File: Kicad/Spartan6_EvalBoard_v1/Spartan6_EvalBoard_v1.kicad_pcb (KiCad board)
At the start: 2 copper layers, 1 part, among them CON1 USB-MINI-B

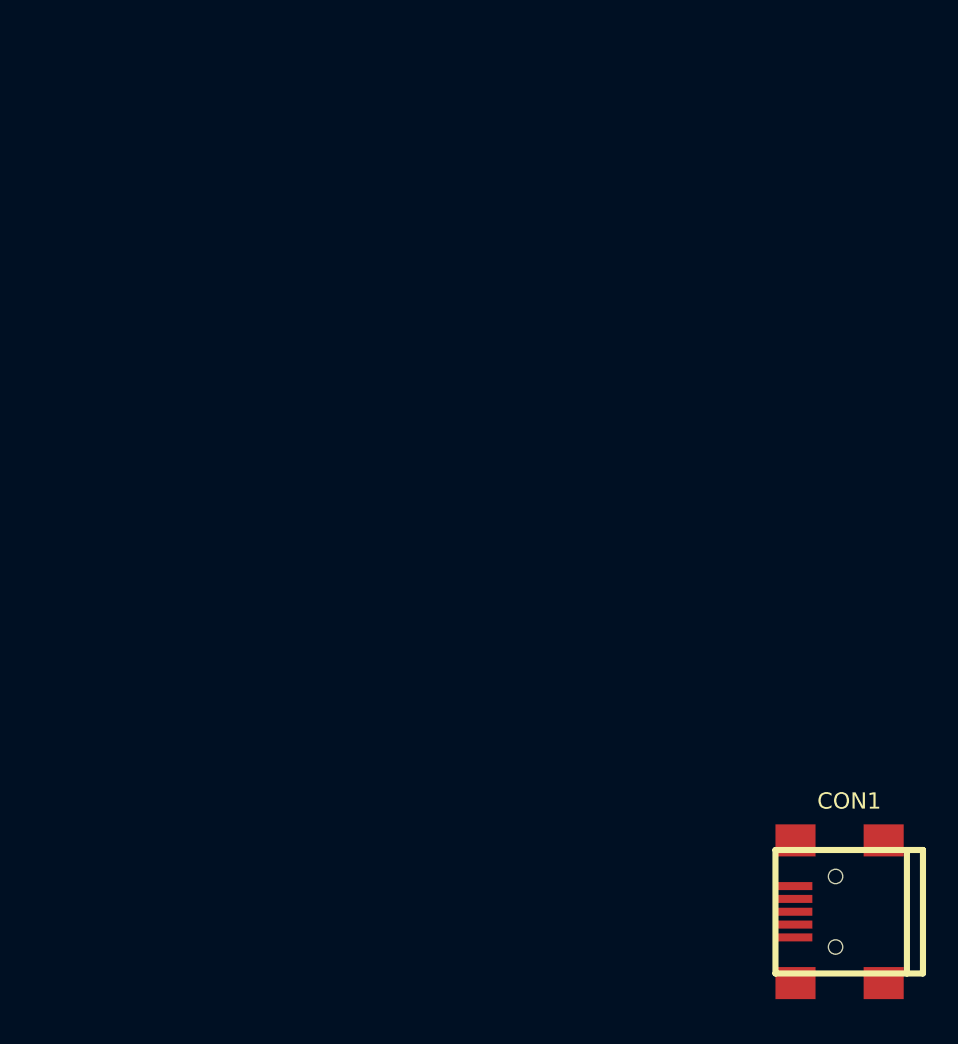
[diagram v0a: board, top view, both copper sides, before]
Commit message: Schematic and netllist created
The correct fpga connection to connector will have to be carried out.
Some more footprints need to be created.
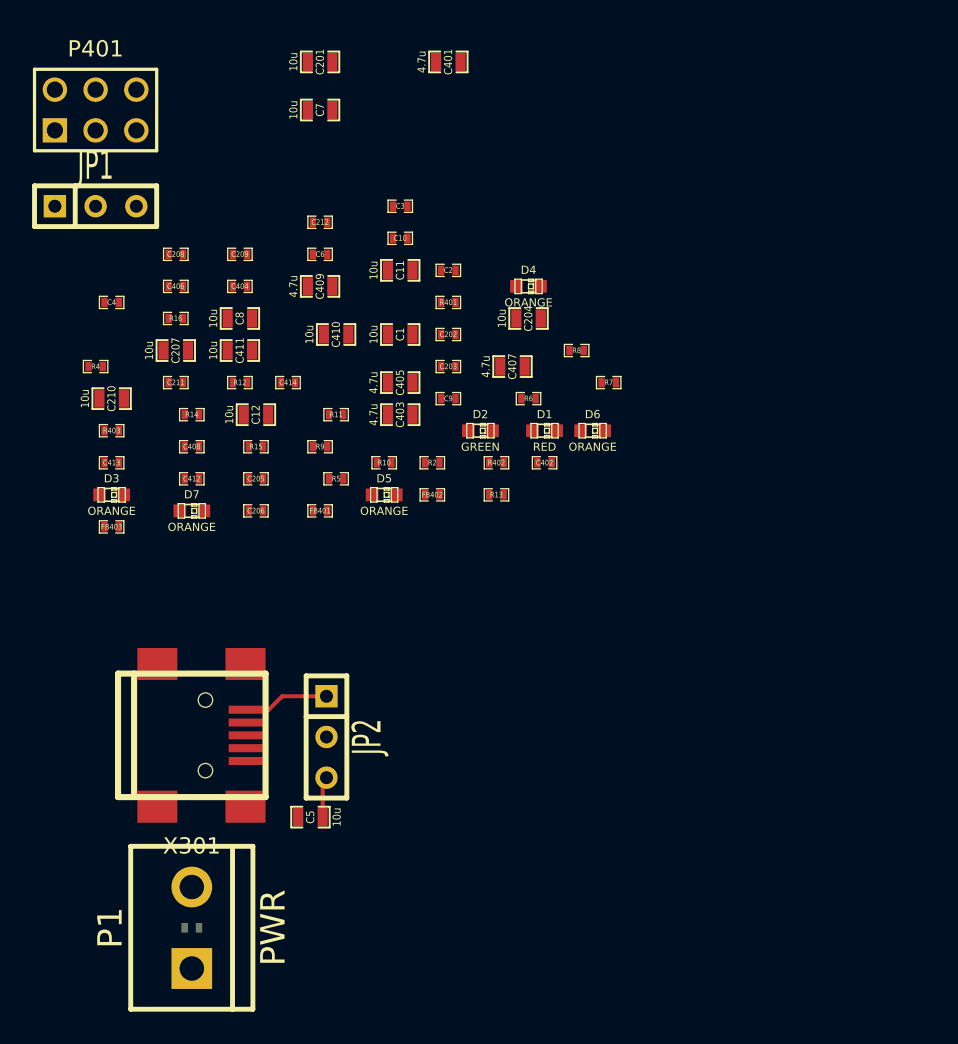
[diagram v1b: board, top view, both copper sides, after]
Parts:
- removed CON1: USB-MINI-B, USB_MINI_B
- added C1: 10u, SM0603_Capa, F.Cu at (117.0, 82.0)
- added C10: 470p, SM0402_c, F.Cu at (117.0, 76.0)
- added C11: 10u, SM0603_Capa, F.Cu at (117.0, 78.0)
- added C12: 10u, SM0603_Capa, F.Cu at (108.0, 87.0)
- added C2: 1u, SM0402_c, F.Cu at (120.0, 78.0)
- added C201: 10u, SM0603_Capa, F.Cu at (112.0, 65.0)
- added C202: 1u, SM0402_c, F.Cu at (120.0, 82.0)
- added C203: 100n, SM0402_c, F.Cu at (120.0, 84.0)
- added C204: 10u, SM0603_Capa, F.Cu at (125.0, 81.0)
- added C205: 1u, SM0402_c, F.Cu at (108.0, 91.0)
- added C206: 100n, SM0402_c, F.Cu at (108.0, 93.0)
- added C207: 10u, SM0603_Capa, F.Cu at (103.0, 83.0)
- added C208: 1u, SM0402_c, F.Cu at (103.0, 77.0)
- added C209: 100n, SM0402_c, F.Cu at (107.0, 77.0)
- added C210: 10u, SM0603_Capa, F.Cu at (99.0, 86.0)
- added C211: 1u, SM0402_c, F.Cu at (103.0, 85.0)
- added C212: 100n, SM0402_c, F.Cu at (112.0, 75.0)
- added C3: 1u, SM0402_c, F.Cu at (117.0, 74.0)
- added C4: 3.3n, SM0402_c, F.Cu at (99.0, 80.0)
- added C401: 4.7u, SM0603_Capa, F.Cu at (120.0, 65.0)
- added C402: 470n, SM0402_c, F.Cu at (126.0, 90.0)
- added C403: 4.7u, SM0603_Capa, F.Cu at (117.0, 87.0)
- added C404: 470n, SM0402_c, F.Cu at (107.0, 79.0)
- added C405: 4.7u, SM0603_Capa, F.Cu at (117.0, 85.0)
- added C406: 470n, SM0402_c, F.Cu at (103.0, 79.0)
- added C407: 4.7u, SM0603_Capa, F.Cu at (124.0, 84.0)
- added C408: 470n, SM0402_c, F.Cu at (104.0, 89.0)
- added C409: 4.7u, SM0603_Capa, F.Cu at (112.0, 79.0)
- added C410: 10u, SM0603_Capa, F.Cu at (113.0, 82.0)
- added C411: 10u, SM0603_Capa, F.Cu at (107.0, 83.0)
- added C412: 100n, SM0402_c, F.Cu at (104.0, 91.0)
- added C413: 100n, SM0402_c, F.Cu at (99.0, 90.0)
- added C414: 100n, SM0402_c, F.Cu at (110.0, 85.0)
- added C5: 10u, SM0603_Capa, F.Cu at (111.4, 112.1)
- added C6: 100n, SM0402_c, F.Cu at (112.0, 77.0)
- added C7: 10u, SM0603_Capa, F.Cu at (112.0, 68.0)
- added C8: 10u, SM0603_Capa, F.Cu at (107.0, 81.0)
- added C9: 470p, SM0402_c, F.Cu at (120.0, 86.0)
- added D1: RED, LED-0603, F.Cu at (126.0, 88.0)
- added D2: GREEN, LED-0603, F.Cu at (122.0, 88.0)
- added D3: ORANGE, LED-0603, F.Cu at (99.0, 92.0)
- added D4: ORANGE, LED-0603, F.Cu at (125.0, 79.0)
- added D5: ORANGE, LED-0603, F.Cu at (116.0, 92.0)
- added D6: ORANGE, LED-0603, F.Cu at (129.0, 88.0)
- added D7: ORANGE, LED-0603, F.Cu at (104.0, 93.0)
- added FB301: F, SM0402, B.Cu at (104.0, 119.0)
- added FB401: F, SM0402, F.Cu at (112.0, 93.0)
- added FB402: F, SM0402, F.Cu at (119.0, 92.0)
- added FB403: F, SM0402, F.Cu at (99.0, 94.0)
- added JP1: JUMPER3, SIL-3, F.Cu at (98.0, 74.0)
- added JP2: JUMPER3, SIL-3, F.Cu at (112.4, 107.1)
- added P1: PWR, bornier2, F.Cu at (104.0, 119.0)
- added P401: CONN_3X2, pin_array_3x2, F.Cu at (98.0, 68.0)
- added R10: 1.2k, SM0402_r, F.Cu at (116.0, 90.0)
- added R11: 4.7k, SM0402_r, F.Cu at (113.0, 87.0)
- added R12: 1.2k, SM0402_r, F.Cu at (107.0, 85.0)
- added R13: 120k, SM0402_r, F.Cu at (123.0, 92.0)
- added R14: 154k, SM0402_r, F.Cu at (104.0, 87.0)
- added R15: 120k, SM0402_r, F.Cu at (108.0, 89.0)
- added R16: 30.9k, SM0402_r, F.Cu at (103.0, 81.0)
- added R2: 1.2k, SM0402_r, F.Cu at (119.0, 90.0)
- added R4: 1.2k, SM0402_r, F.Cu at (98.0, 84.0)
- added R401: 10K, SM0402_r, F.Cu at (120.0, 80.0)
- added R402: 1K, SM0402_r, F.Cu at (123.0, 90.0)
- added R403: 1K, SM0402_r, F.Cu at (99.0, 88.0)
- added R5: 10k, SM0402_r, F.Cu at (113.0, 91.0)
- added R6: 47k, SM0402_r, F.Cu at (125.0, 86.0)
- added R7: 1.2k, SM0402_r, F.Cu at (130.0, 85.0)
- added R8: 1.2k, SM0402_r, F.Cu at (128.0, 83.0)
- added R9: 1.2k, SM0402_r, F.Cu at (112.0, 89.0)
- added X301: USBMICRO, USB_MINI_B, F.Cu at (104.0, 107.0)
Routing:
- net /POWER/5V_USB: track 0.00 -> 5.30 mm
- net /POWER/5V_SWITCHER: track 0.00 -> 2.56 mm
